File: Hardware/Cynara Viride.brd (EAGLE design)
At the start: 160 x 100 mm, 171 parts, among them Q1 TXC-7B, Q2 TXC-7WNEO, SW1 430181038816, SW2 , T1 PDTC143, T2 PDTC143, T3 PDTC143, T4 PDTC143, T5 PDTC143, U1 TM4C129EN, U2 MCP1826S 3V3, U3 LM4132 3V3, U4 XC6SLX9-3TQG, U5 M25P16-SO8, U6 MCP1826S 1V2, U7 , X1 EDGE 50p, X11 SOCK2X17, X12 SOCK2X17, X13 SOCK2X17, X2 EDGE 50p, X23 debug xilinx, X24 debug 10p, X3 EDGE 50p, X4 EDGE 50p, X5 MicroMatch 24, X6 USB C socket, X7 SOCK2X17, X8 RJ45-LAN-10/100

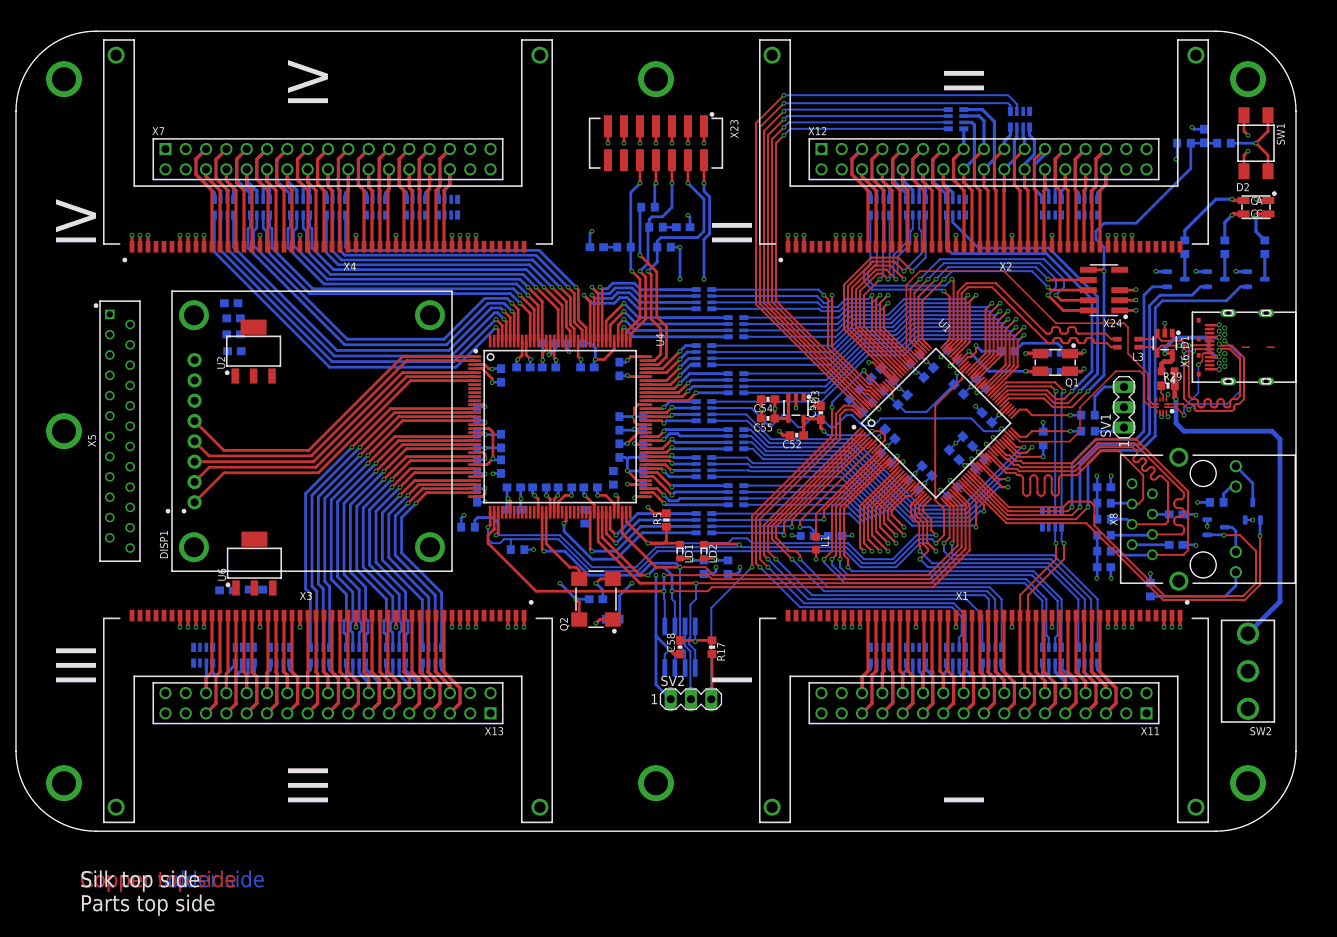
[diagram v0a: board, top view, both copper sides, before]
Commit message: [WIP] Moved FPGA and MCU to make space for Ethernet and USB.
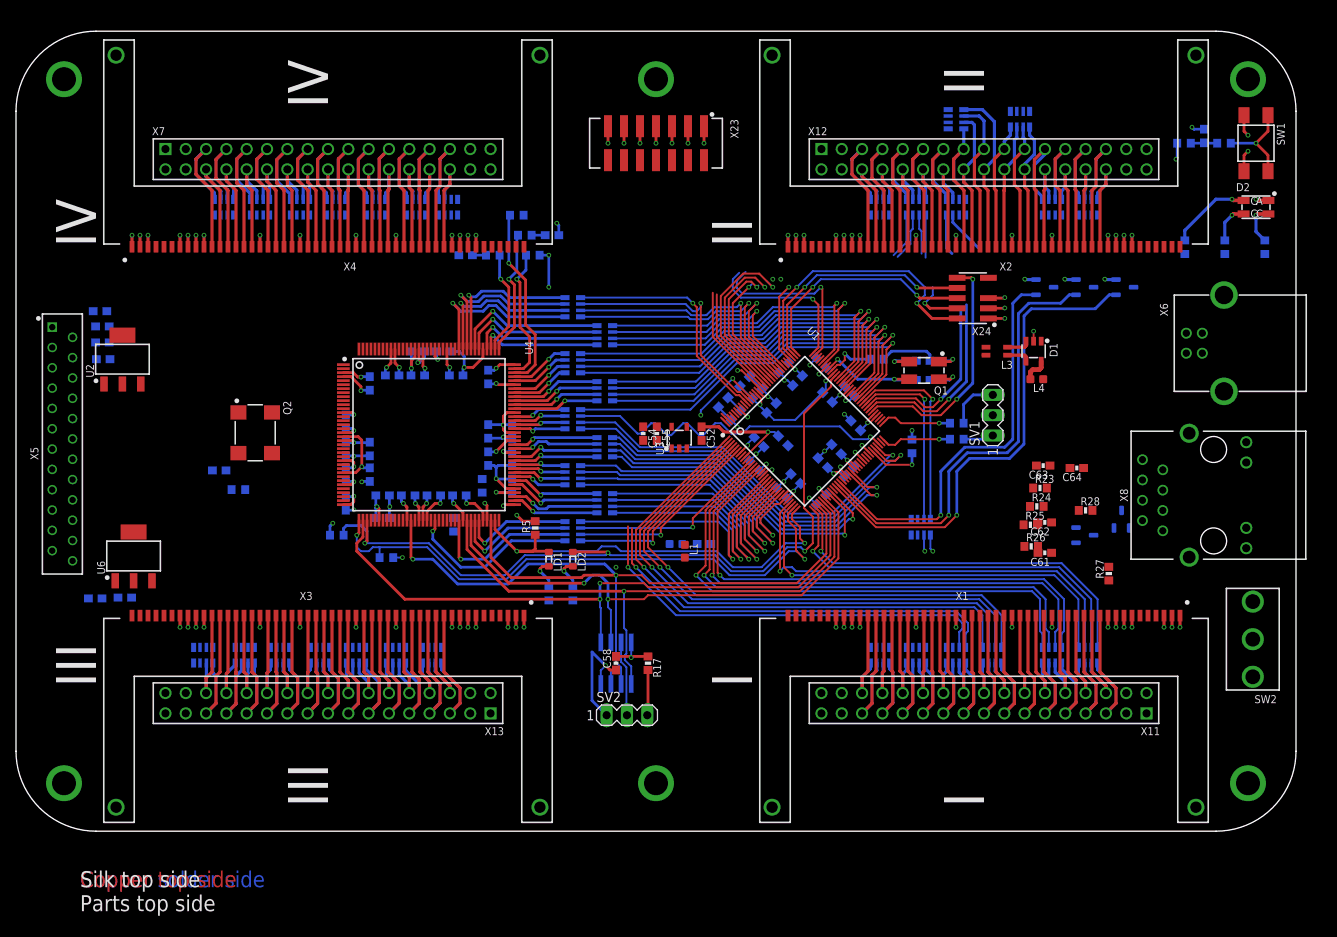
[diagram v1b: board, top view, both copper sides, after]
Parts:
- removed DISP1: (no value), Cynara-Misc:ADAFRUIT_OLED
- removed R29: 900k, Cynara-Passives:R0603
- removed U7: (no value), Cynara-IntegratedCircuits:TUSB320
- X6: value USB C socket -> (none); device Cynara-Connectors:USB-C-RECEPTICAL(632723100011) -> Cynara-Connectors:61400416121
- moved C59 49.8 mm to (25.4, 45.1)
- moved R18 49.5 mm to (27.8, 42.7)
- moved Q2 47.4 mm to (29.9, 49.8), turned to 270 degrees
- moved R2 19.7 mm to (69.6, 29.7)
- moved R4 19.7 mm to (66.6, 29.7)
- moved C1 16.4 mm to (92.9, 48.7)
- moved C10 16.4 mm to (104.2, 55.0)
- moved C13 16.4 mm to (90.0, 52.0)
- moved C15 16.4 mm to (67.0, 74.5)
- moved C16 16.4 mm to (97.7, 56.3)
- moved C19 16.4 mm to (44.2, 44.6)
- moved C21 16.4 mm to (59.0, 46.6)
- moved C22 16.4 mm to (49.0, 42.0)
- moved C23 16.4 mm to (41.2, 47.8)
- moved C24 16.4 mm to (44.2, 47.8)
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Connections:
- removed net 3.3V: DISP1.6
- removed net CC1: U7.1, X6.A5
- removed net CC2: U7.2, X6.B5
- removed net N$18: R29.1, U7.4
- net +3.3V: no longer DISP1.7, U7.12
- net 5V_USB: no longer R29.2
- net D_N: no longer X6.A7, X6.B7
- net D_P: no longer X6.A6, X6.B6
- net GND: now also X6.4; no longer DISP1.8, U7.10, U7.11, U7.3, X6.A1, X6.A12, X6.B1, X6.B12, X6.GND1, X6.GND2
- net OLED_CS: no longer DISP1.5
- net OLED_DC: no longer DISP1.3
- net OLED_MOSI: no longer DISP1.1
- net OLED_RST: no longer DISP1.4
- net OLED_SCLK: no longer DISP1.2
- net USB_DETECT1: no longer U7.7
- net USB_DETECT2: no longer U7.8
- net VBUS: no longer X6.A4, X6.A9, X6.B4, X6.B9
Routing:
- net MCU_II_P: track 76.8 -> 0.00 mm, vias 1 -> 0
- net MCU_II_O: track 73.9 -> 0.00 mm, vias 1 -> 0
- net MCU_II_N: track 63.8 -> 0.00 mm, vias 1 -> 0
- net MCU_II_M: track 62.3 -> 0.00 mm, vias 1 -> 0
- net +3.3V: track 194.2 -> 132.4 mm, vias 49 -> 35
- net MCU_II_L: track 60.9 -> 0.00 mm, vias 1 -> 0
- net MCU_II_K: track 59.4 -> 0.00 mm, vias 1 -> 0
- net PF4_ETH: track 55.3 -> 0.00 mm, vias 1 -> 0
- net USB_DETECT1: track 52.0 -> 0.00 mm
- net PF0_ETH: track 51.9 -> 0.00 mm, vias 1 -> 0
- net FPGA_IV_B: track 49.8 -> 0.00 mm, vias 1 -> 0
- net FPGA_IV_C: track 49.8 -> 0.00 mm, vias 1 -> 0
- net FPGA_IV_A: track 49.7 -> 0.00 mm, vias 1 -> 0
- net FPGA_IV_D: track 49.6 -> 0.00 mm, vias 1 -> 0
- net FPGA_IV_E: track 48.7 -> 0.00 mm, vias 1 -> 0
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
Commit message: Layout for Ethernet and USB 2.0. Fixed problem with VREFA+ being too close to EPI clock signal.
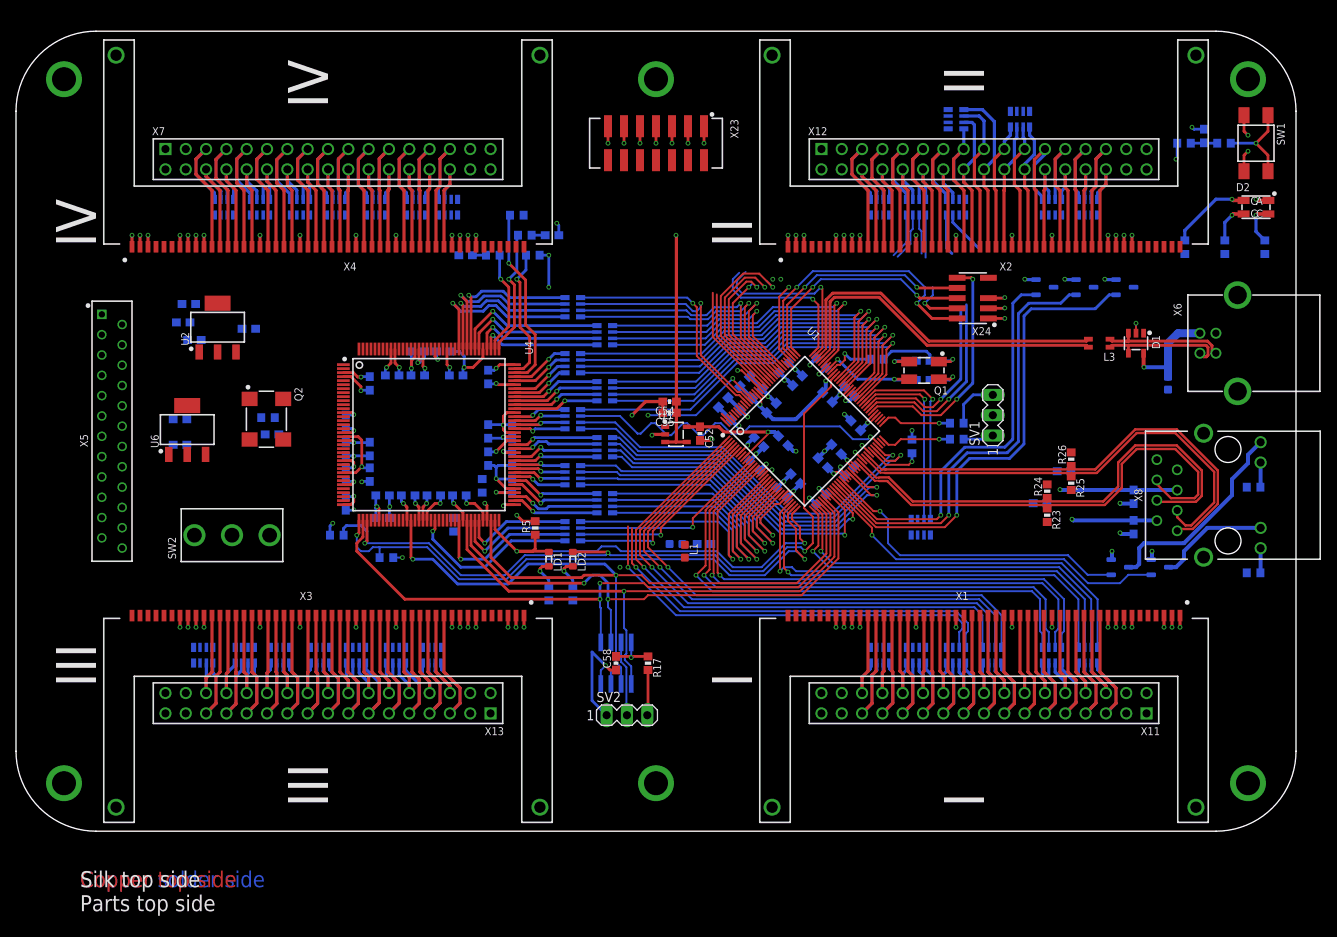
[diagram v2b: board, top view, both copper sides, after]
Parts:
- moved SW2 128.3 mm to (27.0, 37.0), turned to 90 degrees
- moved C43 24.8 mm to (20.5, 51.5)
- moved R28 22.4 mm to (154.7, 32.3), flipped to the bottom
- moved R27 21.1 mm to (154.7, 43.0), flipped to the bottom, turned to 0 degrees
- moved C44 20.3 mm to (20.5, 48.3)
- moved C57 18.6 mm to (29.1, 62.8)
- moved U6 17.2 mm to (21.4, 50.2)
- moved L4 16.4 mm to (144.0, 56.0), flipped to the bottom, turned to 90 degrees
- moved C61 13.1 mm to (139.7, 41.8), flipped to the bottom, turned to 270 degrees
- moved L3 12.8 mm to (135.4, 61.0)
- moved D1 12.8 mm to (140.0, 61.0)
- moved U2 12.6 mm to (25.2, 63.0)
- moved R26 12.0 mm to (131.9, 46.5), turned to 90 degrees
- moved C56 11.5 mm to (22.3, 61.4)
- moved C17 11.1 mm to (21.6, 65.9)
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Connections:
- removed net N$22: T5.3, X8.12
- removed net N$23: R27.1, X8.9
- removed net N$24: R28.1, X8.11
- new net N$14: T4.3, X8.12
- new net N$18: R28.1, X8.9
- new net N$6: R27.1, X8.11
- net D_N: now also X6.2
- net D_P: now also X6.3
- net N$21: now also T5.3; no longer T4.3
- net VBUS: now also X6.1
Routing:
- net ETH_PAIR1_N: track 0.00 -> 60.3 mm
- net ETH_PAIR1_P: track 0.00 -> 60.2 mm
- net ETH_PAIR0_P: track 0.00 -> 60.0 mm
- net ETH_PAIR0_N: track 0.00 -> 59.8 mm
- net PF0_ETH: track 0.00 -> 45.5 mm, vias 0 -> 1
- net USB0D_P: track 0.05 -> 43.3 mm
- net USB0D_N: track 0.45 -> 42.8 mm
- net PF4_ETH: track 0.00 -> 40.2 mm, vias 0 -> 1
- net +5V: track 19.0 -> 47.6 mm, vias 13 -> 14
- net N$14: track 0.00 -> 25.9 mm
- net +3.3V: track 132.4 -> 156.6 mm, vias 35 -> 37
- net GND: track 224.8 -> 241.1 mm, vias 101 -> 109
- net N$21: track 0.00 -> 14.1 mm
- net D_N: track 2.96 -> 15.7 mm
- net D_P: track 2.96 -> 15.6 mm
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
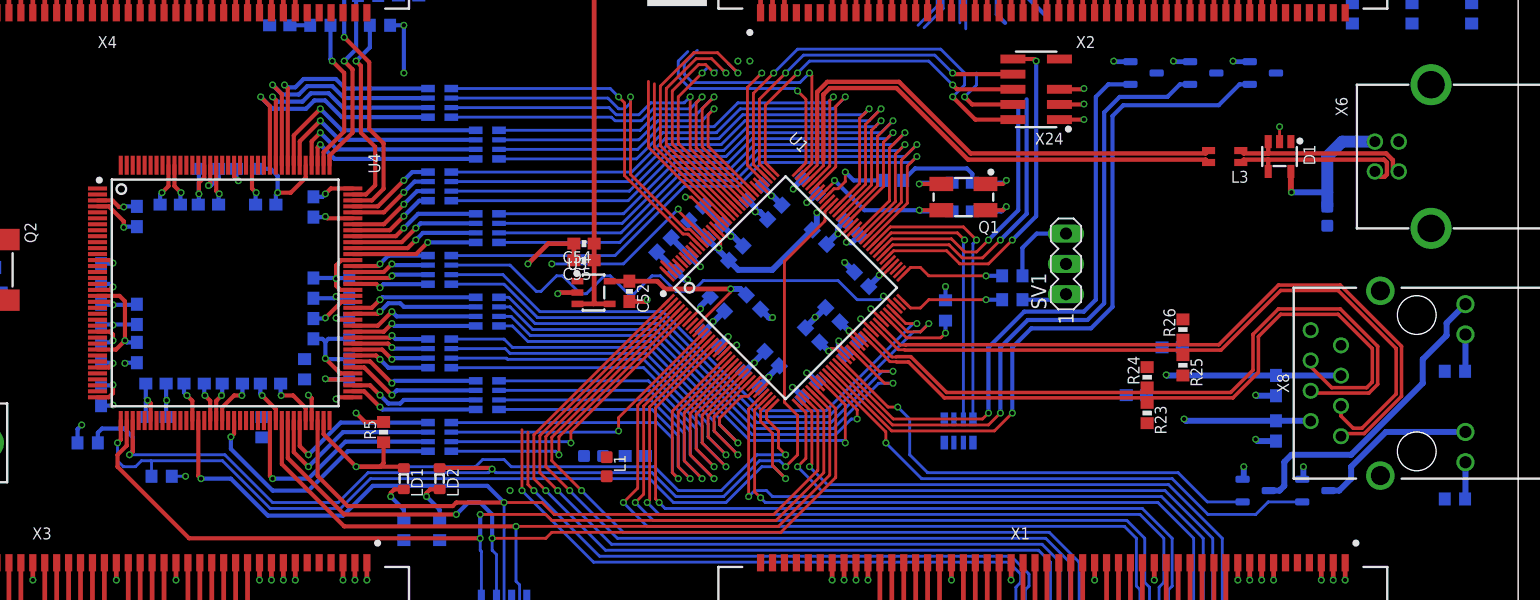
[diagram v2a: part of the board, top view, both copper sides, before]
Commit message: FPGA and C's around the FPGA are snapped to grid again. Small reroute of USB differential pair.
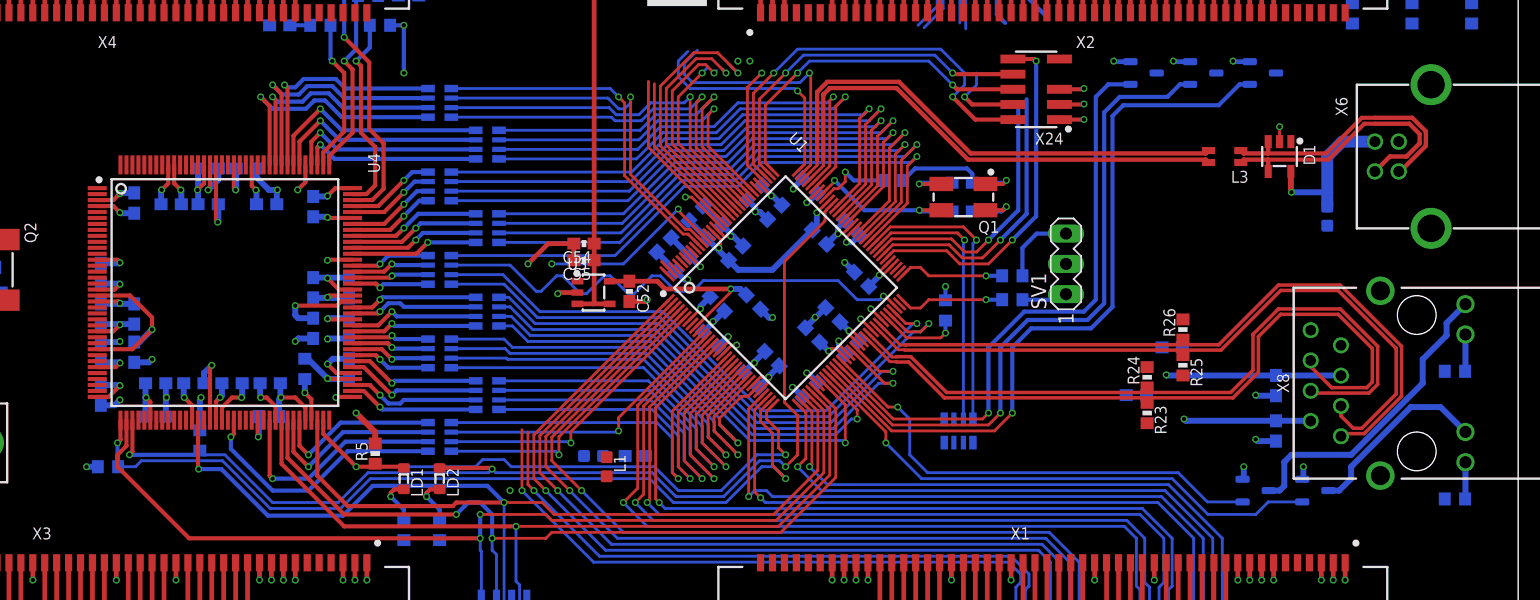
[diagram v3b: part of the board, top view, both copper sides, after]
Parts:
- moved R3 9.40 mm to (49.5, 37.2), turned to 90 degrees
- moved R1 4.57 mm to (41.8, 35.0), turned to 180 degrees
- moved R5 1.93 mm to (64.2, 36.1)
- moved C41 1.15 mm to (44.0, 57.1)
- moved R7 1.07 mm to (55.3, 39.2), turned to 0 degrees
- moved C19 0.22 mm to (44.0, 44.6)
- moved C24 0.22 mm to (44.0, 47.8)
- moved C31 0.08 mm to (47.1, 57.0)
- moved C32 0.08 mm to (55.1, 57.0)
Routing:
- net +1.2V: track 20.3 -> 33.9 mm
- net +3.3V: track 156.6 -> 167.5 mm
- net D_N: track 15.7 -> 23.2 mm
- net D_P: track 15.6 -> 22.7 mm
- net INIT: track 98.0 -> 92.5 mm
- net DONE: track 56.8 -> 52.9 mm
- net M1: track 0.00 -> 3.14 mm, vias 0 -> 1
- net N$21: track 14.1 -> 15.8 mm
- net M0: track 2.24 -> 3.68 mm
- net PROGRAM: track 74.0 -> 73.0 mm
- net GND: track 241.1 -> 241.4 mm, vias 109 -> 113

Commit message: Fixed trace width and spacing issue after reroute of USB differential pair.
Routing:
- net PETAL_I_I: track 13.1 -> 31.1 mm, vias 0 -> 1
- net PETAL_I_J: track 9.92 -> 27.9 mm, vias 0 -> 1
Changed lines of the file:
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@@
 <contactref element="RA12" pad="1A"/>
 <wire x1="126.5" y1="26.95" x2="126.5" y2="19.9" width="0.4" layer="1"/>
-<wire x1="126.5" y1="26.95" x2="114.3" y2="37.025" width="0" layer="19" extent="1-16"/>
+<wire x1="114.3" y1="37.025" x2="114.3" y2="35.7" width="0.4" layer="16"/>
+<wire x1="114.3" y1="35.7" x2="114.5" y2="35.5" width="0.4" layer="16"/>
+<via x="114.5" y="35.5" extent="1-16" drill="0.35"/>
+<wire x1="114.5" y1="35.5" x2="120.3" y2="29.7" width="0.4" layer="1"/>
+<wire x1="120.3" y1="29.7" x2="125.3" y2="29.7" width="0.4" layer="1"/>
+<wire x1="125.3" y1="29.7" x2="126.5" y2="28.5" width="0.4" layer="1"/>
+<wire x1="126.5" y1="28.5" x2="126.5" y2="26.95" width="0.4" layer="1"/>
 </signal>
 <signal name="PETAL_I_J">
@@
 <contactref element="RA12" pad="2A"/>
 <wire x1="125.5" y1="26.95" x2="125.5" y2="19.9" width="0.4" layer="1"/>
-<wire x1="125.5" y1="26.95" x2="113.5" y2="37.025" width="0" layer="19" extent="1-16"/>
+<wire x1="113.5" y1="37.025" x2="113.5" y2="35.5" width="0.4" layer="16"/>
+<via x="113.5" y="35.5" extent="1-16" drill="0.35"/>
+<wire x1="113.5" y1="35.5" x2="120" y2="29" width="0.4" layer="1"/>
+<wire x1="120" y1="29" x2="125" y2="29" width="0.4" layer="1"/>
+<wire x1="125" y1="29" x2="125.5" y2="28.5" width="0.4" layer="1"/>
+<wire x1="125.5" y1="28.5" x2="125.5" y2="26.95" width="0.4" layer="1"/>
 </signal>
 <signal name="PETAL_I_K">
@@
 <wire x1="136.99" y1="60.74" x2="139.05" y2="60.74" width="0.37" layer="1"/>
 <wire x1="139.05" y1="59.75" x2="139.05" y2="60.74" width="0.37" layer="1"/>
-<wire x1="139.05" y1="60.74" x2="144.09355625" y2="60.74" width="0.35" layer="1"/>
-<wire x1="144.09355625" y1="60.74" x2="147.10355625" y2="63.75" width="0.35" layer="1"/>
-<wire x1="147.10355625" y1="63.75" x2="148" y2="63.75" width="0.35" layer="1"/>
-<wire x1="148" y1="63.75" x2="150.8823" y2="63.75" width="0.37" layer="1"/>
-<wire x1="150.8823" y1="63.75" x2="151.74" y2="62.8923" width="0.37" layer="1"/>
-<wire x1="151.74" y1="62.8923" x2="151.74" y2="62.1077" width="0.37" layer="1"/>
 <wire x1="151.74" y1="62.1077" x2="150.6323" y2="61" width="0.37" layer="1"/>
 <wire x1="150.6323" y1="61" x2="149.24" y2="61" width="0.37" layer="1"/>
 <wire x1="149.24" y1="61" x2="147.99" y2="59.75" width="0.37" layer="1"/>
+<wire x1="139.05" y1="60.74" x2="144.1077" y2="60.74" width="0.37" layer="1"/>
+<wire x1="144.1077" y1="60.74" x2="147.1077" y2="63.74" width="0.37" layer="1"/>
+<wire x1="147.1077" y1="63.74" x2="150.8923" y2="63.74" width="0.37" layer="1"/>
+<wire x1="150.8923" y1="63.74" x2="151.74" y2="62.8923" width="0.37" layer="1"/>
+<wire x1="151.74" y1="62.8923" x2="151.74" y2="62.1077" width="0.37" layer="1"/>
 </signal>
 <signal name="D_P">
@@
 <wire x1="136.99" y1="61.26" x2="139.05" y2="61.26" width="0.37" layer="1"/>
 <wire x1="139.05" y1="62.25" x2="139.05" y2="61.26" width="0.37" layer="1"/>
-<wire x1="139.05" y1="61.26" x2="143.90644375" y2="61.26" width="0.35" layer="1"/>
-<wire x1="143.90644375" y1="61.26" x2="146.89644375" y2="64.25" width="0.35" layer="1"/>
-<wire x1="146.89644375" y1="64.25" x2="148" y2="64.25" width="0.35" layer="1"/>
-<wire x1="148" y1="64.25" x2="151.1177" y2="64.25" width="0.37" layer="1"/>
-<wire x1="151.1177" y1="64.25" x2="152.26" y2="63.1077" width="0.37" layer="1"/>
-<wire x1="152.26" y1="63.1077" x2="152.26" y2="61.8923" width="0.37" layer="1"/>
 <wire x1="152.26" y1="61.8923" x2="150.1177" y2="59.75" width="0.37" layer="1"/>
 <wire x1="150.1177" y1="59.75" x2="149.99" y2="59.75" width="0.37" layer="1"/>
+<wire x1="139.05" y1="61.26" x2="143.8923" y2="61.26" width="0.37" layer="1"/>
+<wire x1="143.8923" y1="61.26" x2="146.8923" y2="64.26" width="0.37" layer="1"/>
+<wire x1="146.8923" y1="64.26" x2="151.1077" y2="64.26" width="0.37" layer="1"/>
+<wire x1="151.1077" y1="64.26" x2="152.26" y2="63.1077" width="0.37" layer="1"/>
+<wire x1="152.26" y1="63.1077" x2="152.26" y2="61.8923" width="0.37" layer="1"/>
 </signal>
 <signal name="N$15">
